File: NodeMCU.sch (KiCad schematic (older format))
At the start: 4 parts, among them J2 Conn_01x15, J3 Conn_01x15

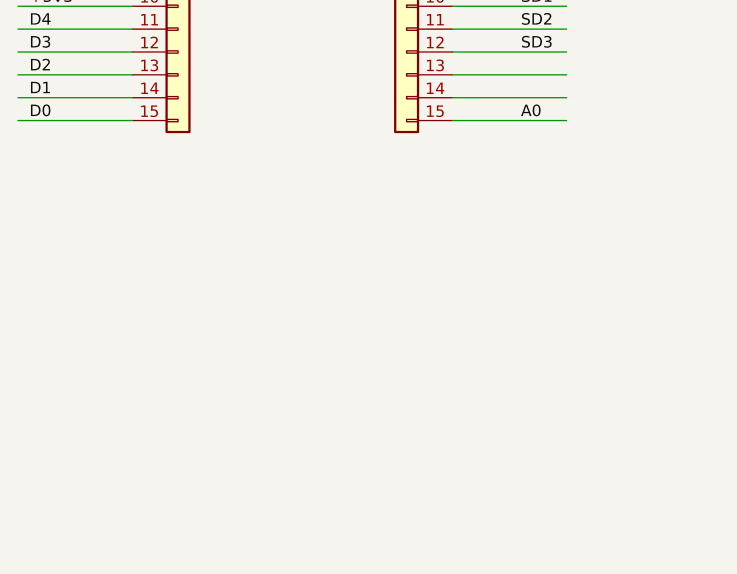
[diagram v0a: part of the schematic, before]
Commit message: added 4-20mA input and PT100 readout
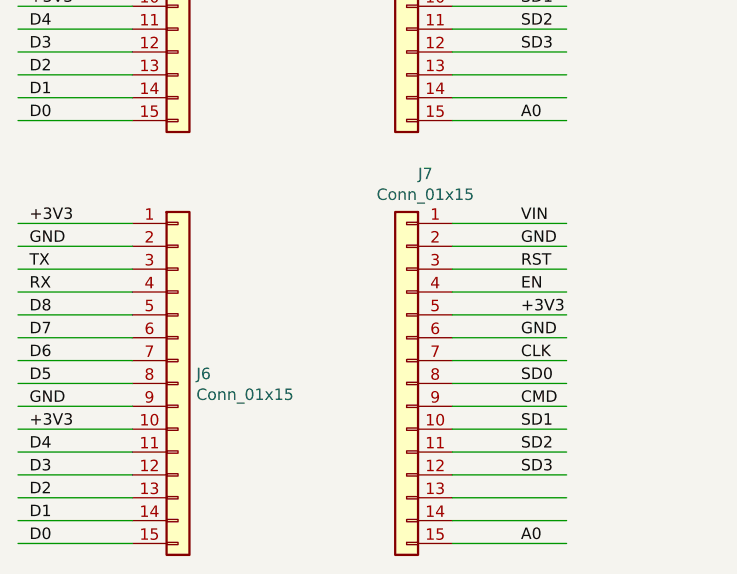
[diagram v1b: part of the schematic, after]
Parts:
- added J6, J7: Conn_01x15, Connector_PinSocket_2.54mm:PinSocket_1x15_P2.54mm_Vertical, symbol Connector_Generic:Conn_01x15
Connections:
- wire segments 38 -> 68
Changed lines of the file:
@@
 $Descr A4 11693 8268
 encoding utf-8
-Sheet 3 4
+Sheet 3 7
 Title "NodeMCU"
 Date ""
 Rev "1"
-Comp ""
+Comp "RWTH Aachen University, Physik 3B"
 Comment1 ""
 Comment2 ""
@@
 Text Label 6150 2050 0    50   ~ 0
 D2
+$Comp
+L Connector_Generic:Conn_01x15 J6
+U 1 1 5ECBADE0
+P 2950 4600
+F 0 "J6" H 3030 4642 50  0000 L CNN
+F 1 "Conn_01x15" H 3030 4551 50  0000 L CNN
+F 2 "Connector_PinSocket_2.54mm:PinSocket_1x15_P2.54mm_Vertical" H 2950 4600 50  0001 C CNN
+F 3 "~" H 2950 4600 50  0001 C CNN
+	1    2950 4600
+	1    0    0    -1
+$EndComp
+$Comp
+L Connector_Generic:Conn_01x15 J7
+U 1 1 5ECBADE6
+P 3950 4600
+F 0 "J7" H 3868 5517 50  0000 C CNN
+F 1 "Conn_01x15" H 3868 5426 50  0000 C CNN
+F 2 "Connector_PinSocket_2.54mm:PinSocket_1x15_P2.54mm_Vertical" H 3950 4600 50  0001 C CNN
+F 3 "~" H 3950 4600 50  0001 C CNN
+	1    3950 4600
+	-1   0    0    -1
+$EndComp
+Wire Wire Line
+	2750 3900 2250 3900
+Wire Wire Line
+	2750 4000 2250 4000
+Wire Wire Line
+	2750 4100 2250 4100
+Wire Wire Line
+	2750 4200 2250 4200
+Wire Wire Line
+	2750 4300 2250 4300
+Wire Wire Line
+	2750 4400 2250 4400
+Wire Wire Line
+	2750 4500 2250 4500
+Wire Wire Line
+	2750 4600 2250 4600
+Wire Wire Line
+	2750 4700 2250 4700
+Wire Wire Line
+	2750 4800 2250 4800
+Wire Wire Line
+	2750 4900 2250 4900
+Wire Wire Line
+	2750 5000 2250 5000
+Wire Wire Line
+	2750 5100 2250 5100
+Wire Wire Line
+	2750 5200 2250 5200
+Wire Wire Line
+	2750 5300 2250 5300
+Wire Wire Line
+	4650 3900 4150 3900
+Wire Wire Line
+	4650 4000 4150 4000
+Wire Wire Line
+	4650 4100 4150 4100
+Wire Wire Line
+	4650 4200 4150 4200
+Wire Wire Line
+	4650 4300 4150 4300
+Wire Wire Line
+	4650 4400 4150 4400
+Wire Wire Line
+	4650 4500 4150 4500
+Wire Wire Line
+	4650 4600 4150 4600
+Wire Wire Line
+	4650 4700 4150 4700
+Wire Wire Line
+	4650 4800 4150 4800
+Wire Wire Line
+	4650 4900 4150 4900
+Wire Wire Line
+	4650 5000 4150 5000
+Wire Wire Line
+	4650 5100 4150 5100
+Wire Wire Line
+	4650 5200 4150 5200
+Wire Wire Line
+	4650 5300 4150 5300
+Text Label 2300 3900 0    50   ~ 0
++3V3
+Text Label 2300 4000 0    50   ~ 0
+GND
+Text Label 2300 4100 0    50   ~ 0
+TX
+Text Label 2300 4200 0    50   ~ 0
+RX
+Text Label 2300 4300 0    50   ~ 0
+D8
+Text Label 2300 4400 0    50   ~ 0
+D7
+Text Label 2300 4500 0    50   ~ 0
+D6
+Text Label 2300 4600 0    50   ~ 0
+D5
+Text Label 2300 4700 0    50   ~ 0
+GND
+Text Label 2300 4800 0    50   ~ 0
++3V3
+Text Label 2300 4900 0    50   ~ 0
+D4
+Text Label 2300 5000 0    50   ~ 0
+D3
+Text Label 2300 5100 0    50   ~ 0
+D2
+Text Label 2300 5200 0    50   ~ 0
+D1
+Text Label 2300 5300 0    50   ~ 0
+D0
+Text Label 4450 3900 0    50   ~ 0
+VIN
+Text Label 4450 4000 0    50   ~ 0
+GND
+Text Label 4450 4100 0    50   ~ 0
+RST
+Text Label 4450 4200 0    50   ~ 0
+EN
+Text Label 4450 4300 0    50   ~ 0
++3V3
+Text Label 4450 4400 0    50   ~ 0
+GND
+Text Label 4450 4500 0    50   ~ 0
+CLK
+Text Label 4450 4600 0    50   ~ 0
+SD0
+Text Label 4450 4700 0    50   ~ 0
+CMD
+Text Label 4450 4800 0    50   ~ 0
+SD1
+Text Label 4450 4900 0    50   ~ 0
+SD2
+Text Label 4450 5000 0    50   ~ 0
+SD3
+Text Label 4450 5300 0    50   ~ 0
+A0
 $EndSCHEMATC

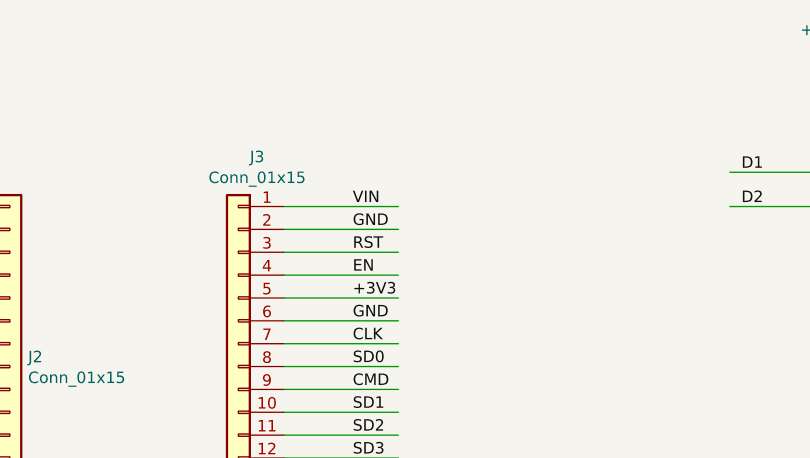
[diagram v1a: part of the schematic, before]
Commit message: added digital output, 24V to 5V voltage regulator
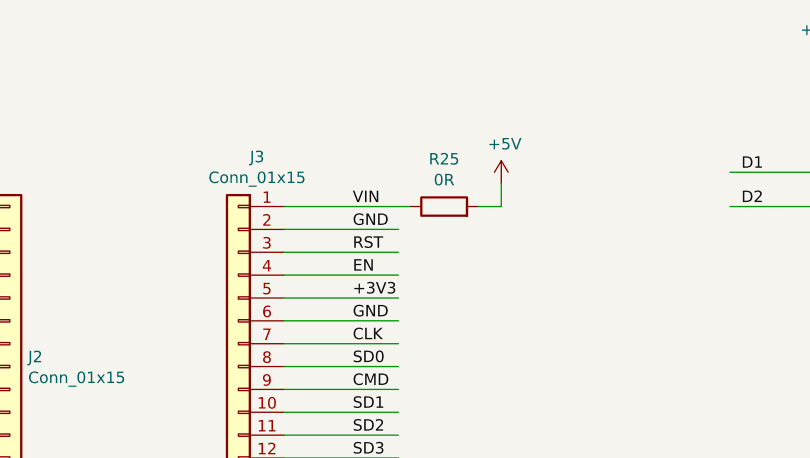
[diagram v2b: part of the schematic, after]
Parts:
- added R25: 0R, Resistor_SMD:R_0603_1608Metric, symbol Device:R
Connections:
- net labels added: +5V
- wire segments 68 -> 70
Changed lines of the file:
@@
 $Descr A4 11693 8268
 encoding utf-8
-Sheet 3 7
+Sheet 2 7
 Title "NodeMCU"
 Date ""
@@
 Wire Wire Line
 	2750 3450 2250 3450
-Wire Wire Line
-	4650 2050 4150 2050
 Wire Wire Line
 	4650 2150 4150 2150
@@
 Text Label 4450 5300 0    50   ~ 0
 A0
+$Comp
+L Device:R R25
+U 1 1 5EE06FEF
+P 4850 2050
+F 0 "R25" V 5057 2050 50  0000 C CNN
+F 1 "0R" V 4966 2050 50  0000 C CNN
+F 2 "Resistor_SMD:R_0603_1608Metric" V 4780 2050 50  0001 C CNN
+F 3 "~" H 4850 2050 50  0001 C CNN
+	1    4850 2050
+	0    -1   -1   0
+$EndComp
+Wire Wire Line
+	4150 2050 4700 2050
+$Comp
+L power:+5V #PWR071
+U 1 1 5EE08F07
+P 5100 1950
+F 0 "#PWR071" H 5100 1800 50  0001 C CNN
+F 1 "+5V" H 5115 2123 50  0000 C CNN
+F 2 "" H 5100 1950 50  0001 C CNN
+F 3 "" H 5100 1950 50  0001 C CNN
+	1    5100 1950
+	1    0    0    -1
+$EndComp
+Wire Wire Line
+	5000 2050 5100 2050
+Wire Wire Line
+	5100 2050 5100 1950
 $EndSCHEMATC
